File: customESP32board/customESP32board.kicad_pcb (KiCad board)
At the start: 2 copper layers, 60 x 60 mm, 47 parts, among them J1 USB_B_Micro, J2 Conn_01x16_Pin, J3 Conn_01x16_Pin, Q1 S8050, Q2 S8050, Q3 BSS138, Q4 BSS138, Q5 BSS138, SW1 SW_Push, SW2 SW_Push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

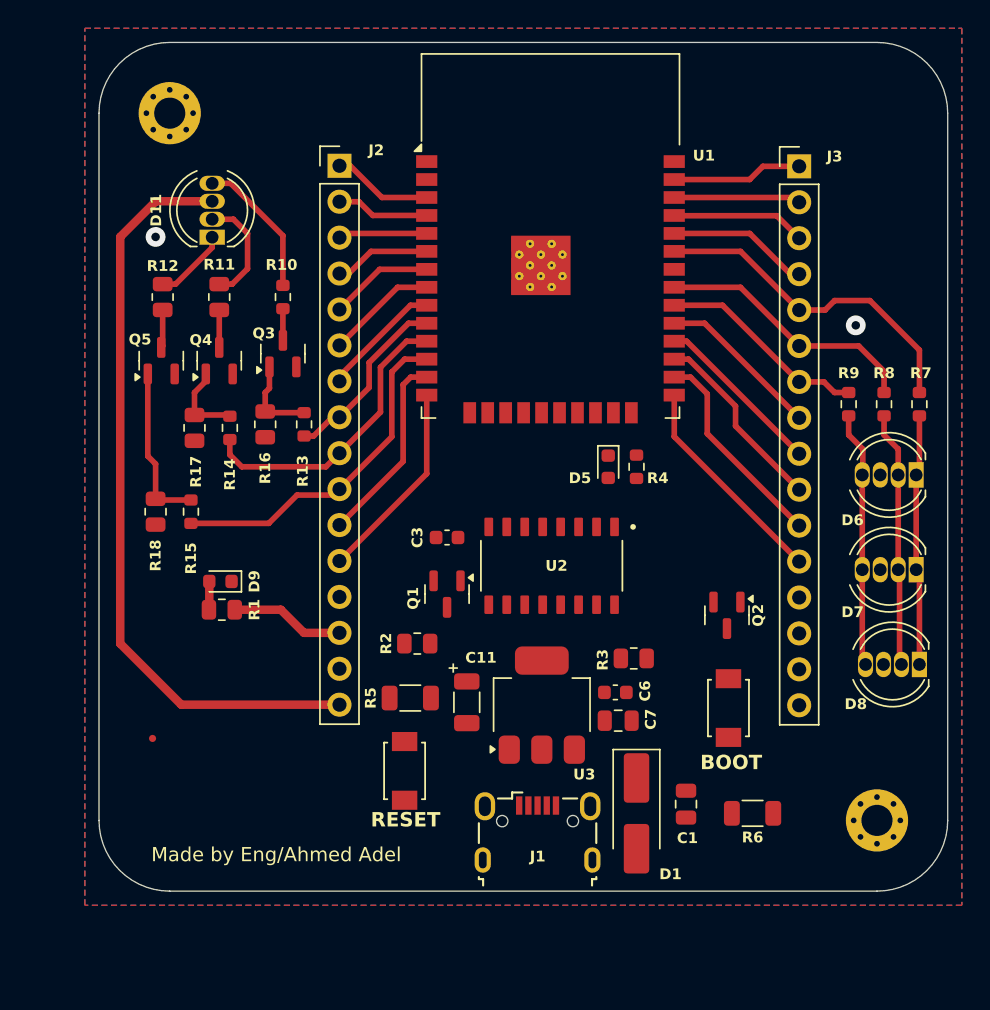
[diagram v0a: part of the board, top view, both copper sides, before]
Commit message: update pcb board size to 65mm x 60mm
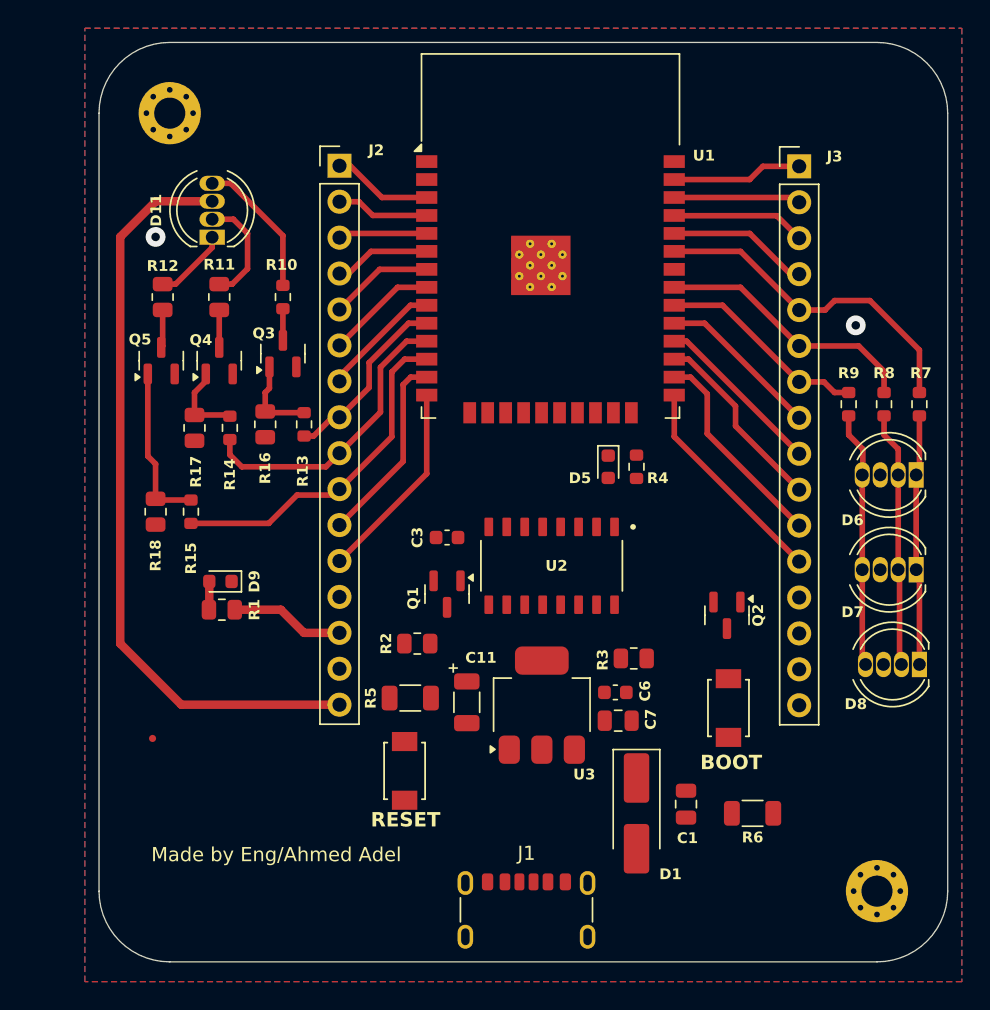
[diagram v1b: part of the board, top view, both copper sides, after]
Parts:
- J1: footprint Connector_USB:USB_Micro-B_Wuerth_629105150521 -> Connector_USB:USB_C_Receptacle_GCT_USB4125-xx-x-0190_6P_TopMnt_Horizontal
- U2: value SOIC127P600X180-16N -> CH340C
- moved J1 6.62 mm to (134.7, 135.9)
- moved H2 5.00 mm to (159.5, 133.5)
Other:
- board size 60 x 60 mm -> 60 x 65 mm

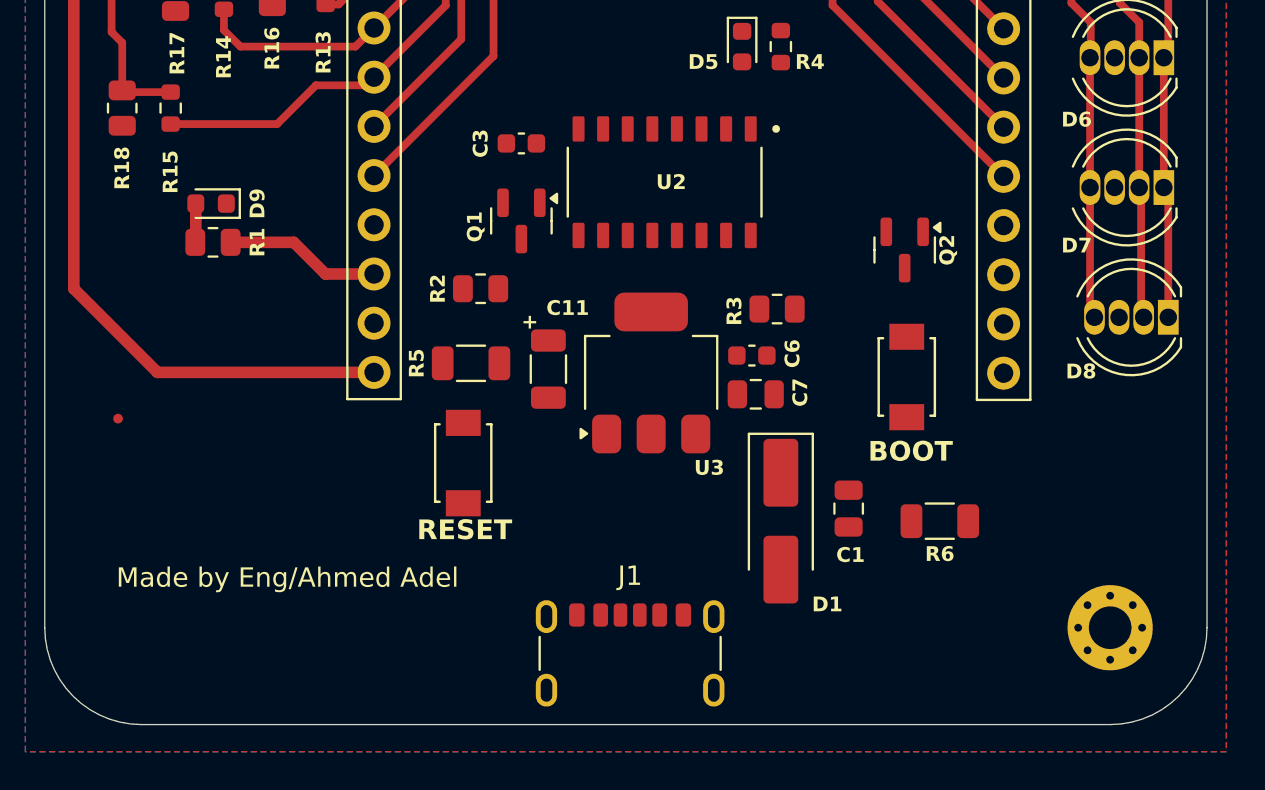
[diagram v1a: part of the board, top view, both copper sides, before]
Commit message: updated D+ and D- routing
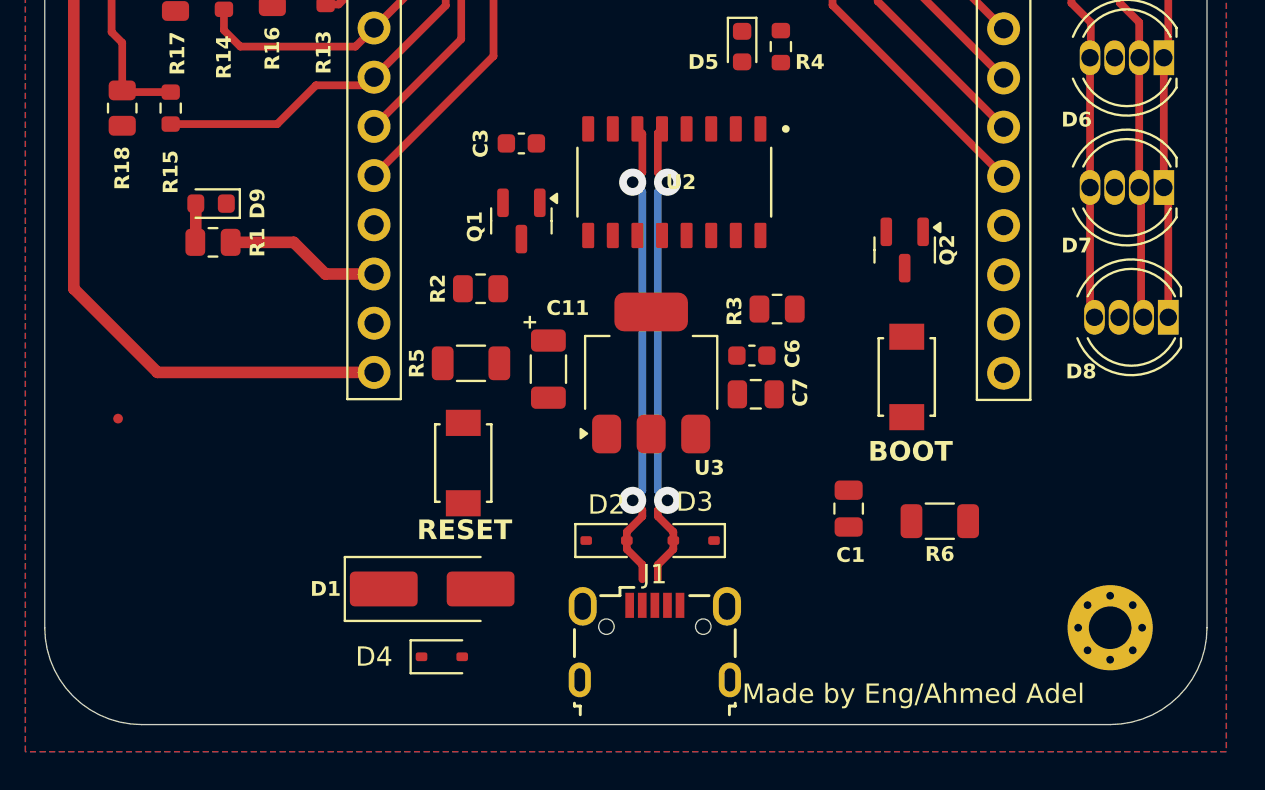
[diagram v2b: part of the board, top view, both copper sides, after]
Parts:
- added D2: SD05_SOD323, Diode_SMD:D_SOD-323, F.Cu at (133.5, 129.0)
- added D3: SD05_SOD323, Diode_SMD:D_SOD-323, F.Cu at (138.0, 129.0)
- added D4: SD05_SOD323, Diode_SMD:D_SOD-323, F.Cu at (125.0, 135.0)
- J1: footprint Connector_USB:USB_C_Receptacle_GCT_USB4125-xx-x-0190_6P_TopMnt_Horizontal -> Connector_USB:USB_Micro-B_Wuerth_629105150521
- moved D1 18.3 mm to (124.5, 131.5), turned to 0 degrees
- moved J1 2.11 mm to (136.0, 134.2)
- moved U2 0.50 mm to (137.0, 110.5)
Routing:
- net UD-: track 0.00 -> 24.8 mm, vias 0 -> 2
- net UD+: track 0.00 -> 24.8 mm, vias 0 -> 2

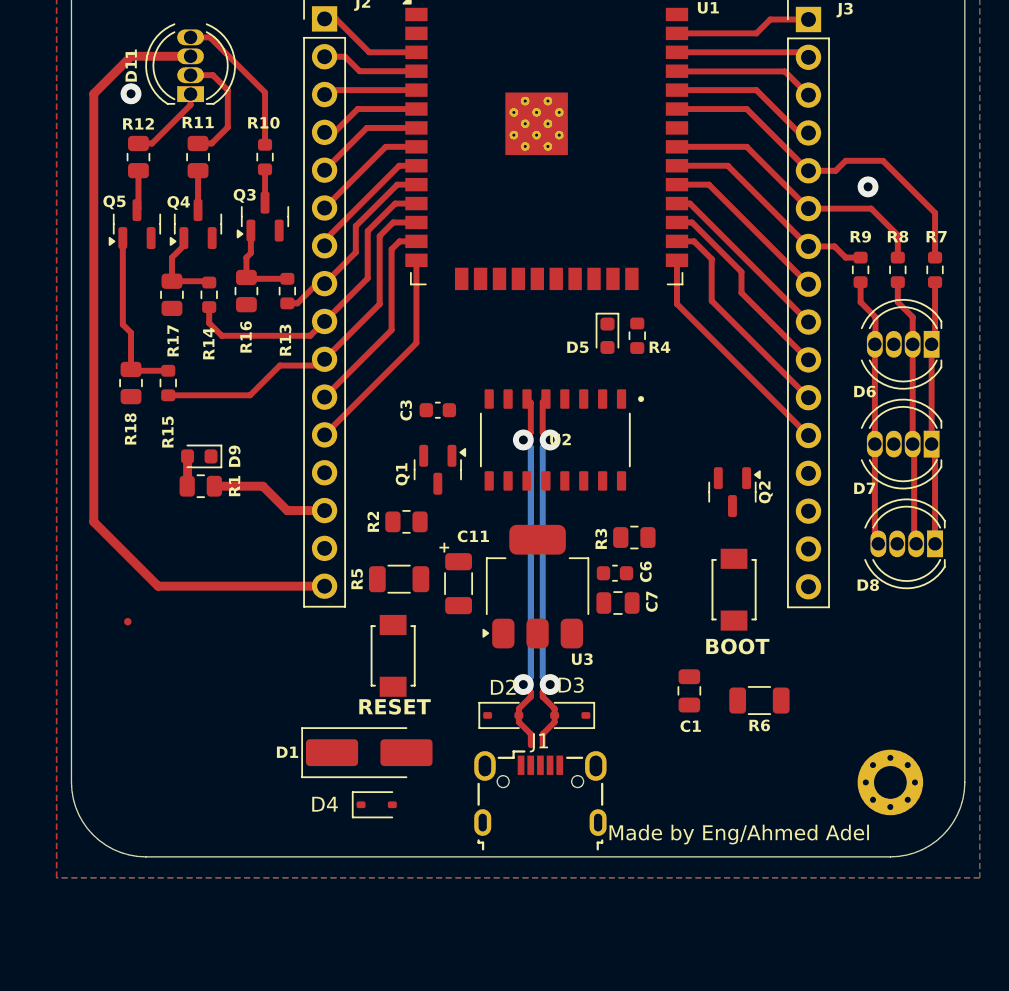
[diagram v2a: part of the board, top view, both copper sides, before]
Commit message: updated connector to USB Type B for production DRC constraints
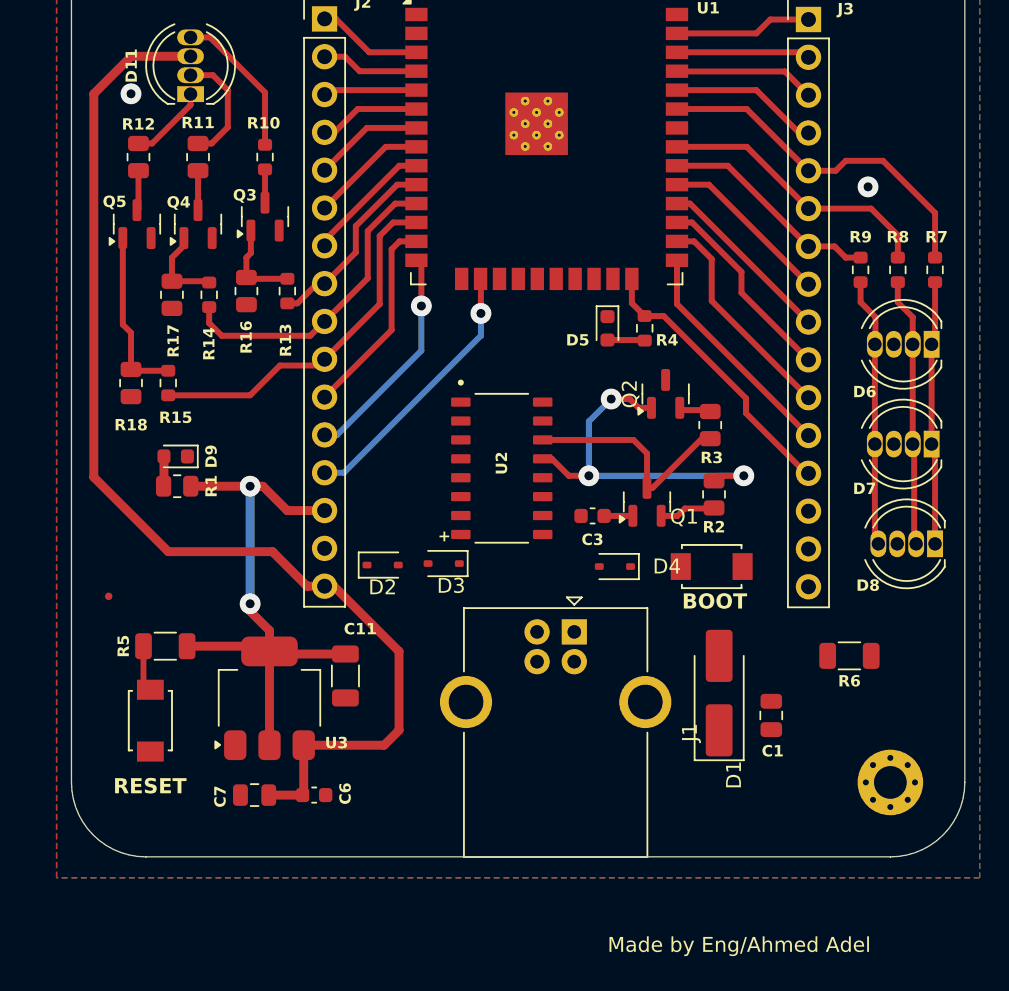
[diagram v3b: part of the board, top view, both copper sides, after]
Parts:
- J1: value USB_B_Micro -> USB_B; footprint Connector_USB:USB_Micro-B_Wuerth_629105150521 -> Connector_USB:USB_B_OST_USB-B1HSxx_Horizontal
- moved C7 27.6 mm to (116.8, 134.3), turned to 180 degrees
- moved C6 25.1 mm to (120.8, 134.3)
- moved D1 23.8 mm to (148.0, 127.5), turned to 90 degrees
- moved D4 22.6 mm to (141.0, 119.0), turned to 180 degrees
- moved R2 20.7 mm to (147.7, 114.2), turned to -90 degrees
- moved U3 19.5 mm to (117.8, 127.8)
- moved SW1 16.9 mm to (109.8, 129.3)
- moved R5 16.3 mm to (110.8, 124.3)
- moved Q1 14.2 mm to (143.2, 114.7), turned to 90 degrees
- moved D3 13.3 mm to (129.5, 118.8)
- moved D2 12.9 mm to (125.4, 118.9)
- moved C3 12.6 mm to (139.5, 115.6)
- moved J1 11.1 mm to (138.3, 123.4), turned to -90 degrees
- moved C11 9.81 mm to (122.9, 126.3)
- moved R3 9.11 mm to (147.4, 109.5), turned to 90 degrees
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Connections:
- J1 pad 4: unconnected-(J1-ID-Pad4) -> GND
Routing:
- net +3V3: track 8.08 -> 38.5 mm, vias 0 -> 2
- net UD-: track 24.8 -> 0.00 mm, vias 2 -> 0
- net DTR: track 0.00 -> 24.8 mm, vias 0 -> 3
- net UD+: track 24.8 -> 0.00 mm, vias 2 -> 0
- net +5V: track 53.6 -> 76.4 mm
- net ESP_IO2: track 0.00 -> 18.8 mm
- net ESP_IO13: track 0.00 -> 18.1 mm, vias 0 -> 1
- net RTS: track 0.00 -> 15.4 mm
- net ESP_EN: track 7.10 -> 12.1 mm
- net Net-(Q1-B): track 0.00 -> 3.77 mm
- net Net-(D5-A): track 0.00 -> 2.52 mm
- net Net-(Q2-B): track 0.00 -> 2.15 mm
- net ESP_IO12: track 14.3 -> 15.0 mm, vias 0 -> 1

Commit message: updated routing, placemennt, new USB B footprint
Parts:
- removed FID1, FID2: Fiducial, Fiducial:Fiducial_0.5mm_Mask1.5mm
- moved SW2 13.4 mm to (159.9, 124.2), turned to 180 degrees
- moved C3 6.74 mm to (134.0, 119.5), turned to 90 degrees
- moved C1 5.64 mm to (149.1, 134.1), turned to 180 degrees
- moved R6 4.13 mm to (152.7, 124.2), turned to 180 degrees
- moved D3 4.10 mm to (125.4, 118.9), turned to 0 degrees
- moved D2 4.00 mm to (129.4, 118.9), turned to 180 degrees
- moved D4 2.98 mm to (143.9, 119.7)
- moved D5 2.94 mm to (138.1, 104.7), turned to 0 degrees
- moved R2 1.90 mm to (148.6, 115.8)
- moved R5 1.38 mm to (111.1, 123.0)
- moved R4 1.00 mm to (142.4, 103.8)
- moved J1 0.97 mm to (137.3, 123.4)
- moved SW1 0.59 mm to (109.6, 129.9)
- moved R9 0.22 mm to (157.5, 99.3)
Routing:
- net +3V3: track 38.5 -> 133.2 mm, vias 2 -> 4
- net ESP_EN: track 12.1 -> 96.4 mm, vias 0 -> 2
- net ESP_U0TX: track 9.50 -> 48.6 mm, vias 0 -> 1
- net ESP_U0RX: track 10.0 -> 42.1 mm, vias 0 -> 1
- net +5V: track 76.4 -> 104.8 mm
- net ESP_IO0: track 15.4 -> 40.7 mm, vias 0 -> 2
- net ESP_IO15: track 0.00 -> 22.6 mm, vias 0 -> 2
- net UD+: track 0.00 -> 20.5 mm
- net Net-(D1-A): track 0.00 -> 20.0 mm
- net UD-: track 0.00 -> 17.9 mm
- net DTR: track 24.8 -> 22.6 mm
- net Net-(Q1-B): track 3.77 -> 5.12 mm
- net ESP_IO2: track 18.8 -> 19.9 mm
- net Net-(D5-A): track 2.52 -> 3.55 mm
- net ESP_IO12: track 15.0 -> 14.3 mm, vias 1 -> 0
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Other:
- board text added: "Made by E/Ahmed Adel"
- board text removed: "Made by Eng/Ahmed Adel"

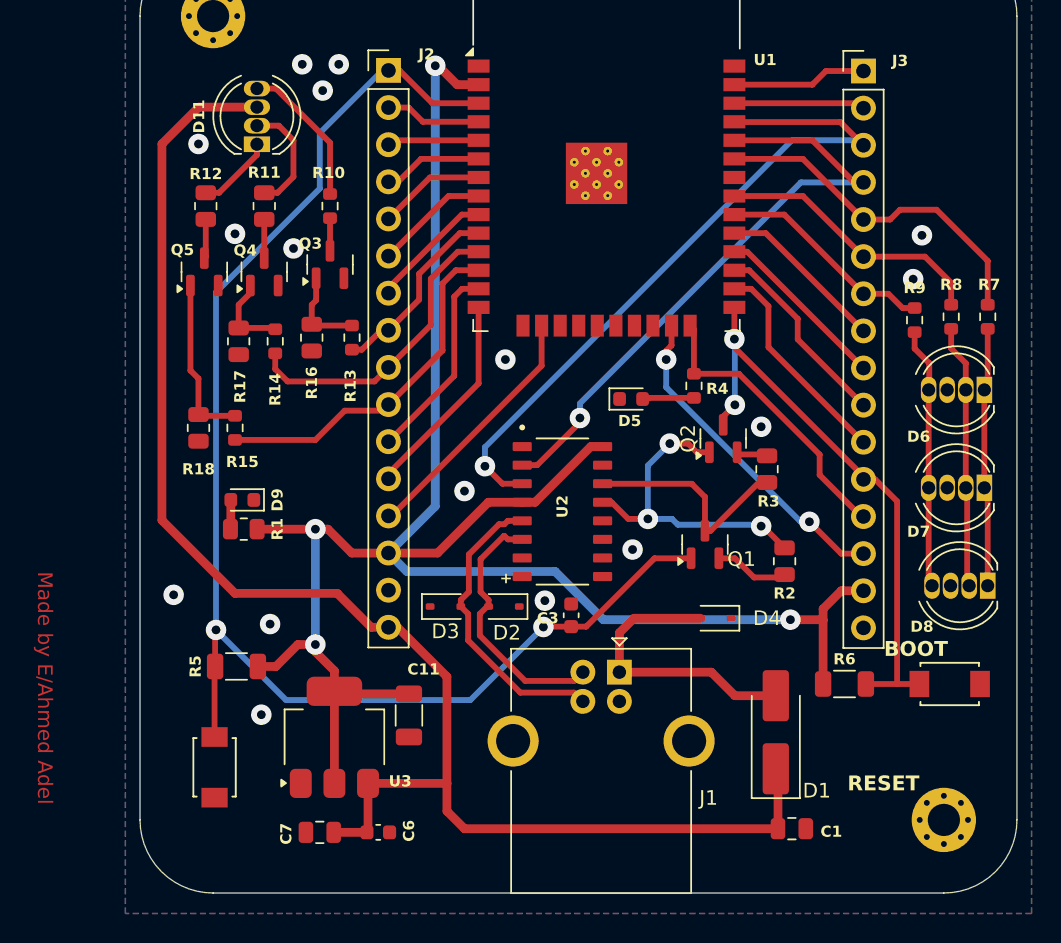
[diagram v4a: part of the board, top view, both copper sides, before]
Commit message: updated routing and placement
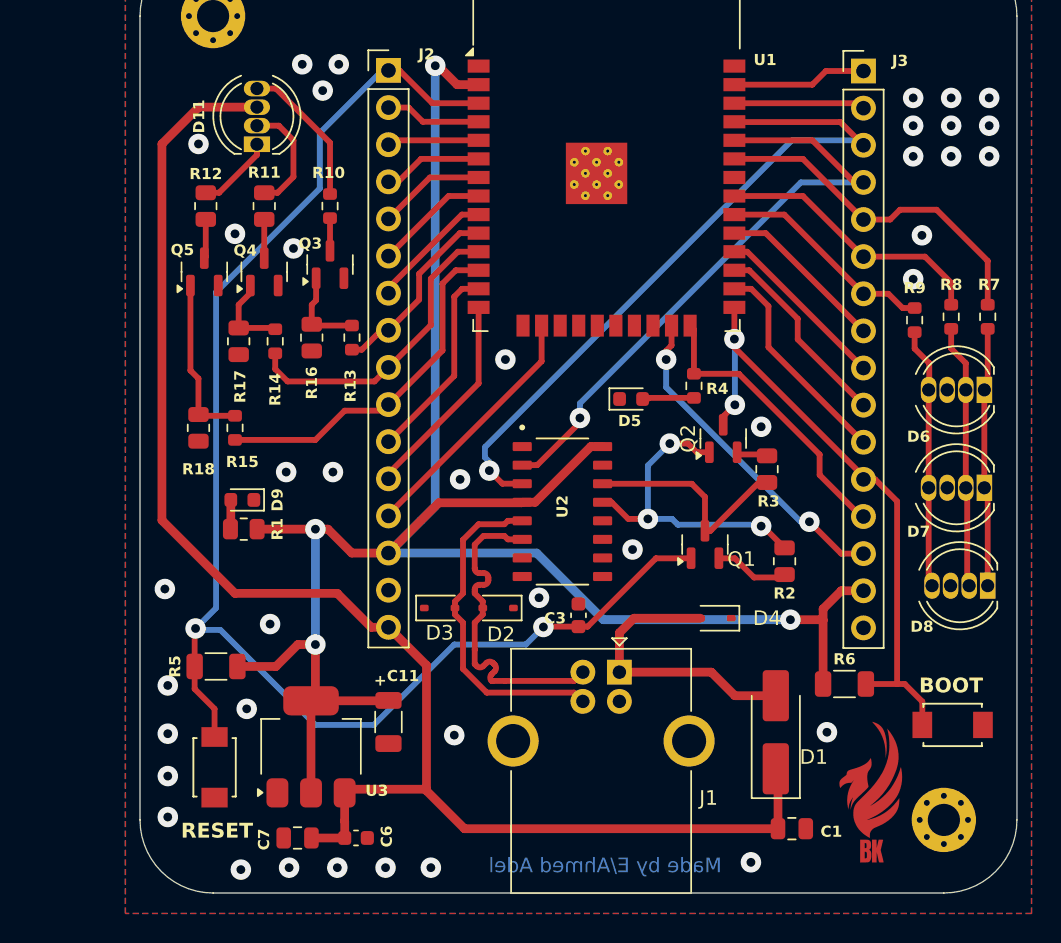
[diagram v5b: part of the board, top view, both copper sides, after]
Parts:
- added G***: LOGO, LOGO, F.Cu at (154.6, 130.9)
- moved SW2 2.81 mm to (160.1, 127.0)
- moved U3 1.73 mm to (116.2, 128.5)
- moved C6 1.57 mm to (119.3, 134.7)
- moved C7 1.57 mm to (115.3, 134.7)
- moved C11 1.47 mm to (121.5, 126.8)
- moved R5 1.40 mm to (109.7, 123.0)
- moved C3 0.50 mm to (134.5, 119.5)
- moved D2 0.41 mm to (129.0, 119.0)
- moved D3 0.41 mm to (125.0, 119.0)
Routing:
- net UD-: track 17.9 -> 22.9 mm
- net ESP_EN: track 96.4 -> 100.4 mm
- net UD+: track 20.5 -> 23.0 mm
- net ESP_IO0: track 40.7 -> 43.0 mm
- net +3V3: track 133.2 -> 135.0 mm
- net GND: vias 16 -> 39
